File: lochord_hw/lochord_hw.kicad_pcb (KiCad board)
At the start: 2 copper layers, 29 x 51.9 mm, 21 parts, among them J1 TYPE-C-31-M-12, J2 Conn_01x20_Pin, J3 Conn_01x20_Pin, SW1 TS-1088-AR02016, SW2 TS-1088-AR02016, U2 ESP32-S3-WROOM-1, U3 LD1117S33TR_SOT223

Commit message: atomic14 pcb design
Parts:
- removed D1: RED, LED_SMD:LED_0603_1608Metric
- removed D2: GREEN, LED_SMD:LED_0603_1608Metric
- removed J2, J3: Conn_01x20_Pin, Connector_PinHeader_2.54mm:PinHeader_1x20_P2.54mm_Vertical
- removed the R5 at (131.8, 69.5)
- added C6: 100nF, Capacitor_SMD:C_0603_1608Metric, F.Cu at (85.7, 87.0)
- added R10: 10K, Resistor_SMD:R_0603_1608Metric, F.Cu at (169.0, 62.3)
- added R11: 10K, Resistor_SMD:R_0603_1608Metric, F.Cu at (169.0, 64.8)
- added R12: 10K, Resistor_SMD:R_0603_1608Metric, F.Cu at (169.0, 67.3)
- added R13: 10K, Resistor_SMD:R_0603_1608Metric, F.Cu at (169.0, 69.9)
- added R14: 10K, Resistor_SMD:R_0603_1608Metric, F.Cu at (169.0, 72.4)
- added R6: 10K, Resistor_SMD:R_0603_1608Metric, F.Cu at (165.0, 67.3)
- added R7: 10K, Resistor_SMD:R_0603_1608Metric, F.Cu at (165.0, 69.9)
- added R8: 10K, Resistor_SMD:R_0603_1608Metric, F.Cu at (165.0, 72.4)
- added R9: 10K, Resistor_SMD:R_0603_1608Metric, F.Cu at (165.0, 74.9)
- added SW10: SW_Push, Switch_Keyboard_Kailh:SW_Kailh_Choc_V2_1.50u, F.Cu at (180.0, 83.5)
- added SW11: SW_Push, Switch_Keyboard_Kailh:SW_Kailh_Choc_V2_1.00u, F.Cu at (204.0, 83.5)
- added SW12: SW_Push, Switch_Keyboard_Kailh:SW_Kailh_Choc_V2_1.50u, F.Cu at (228.5, 83.5)
- added SW13: UI_Encoder, Rotary_Encoder:RotaryEncoder_Alps_EC11E-Switch_Vertical_H20mm_CircularMountingHoles, F.Cu at (117.2, 64.5)
- added SW14: SW_Push, Switch_Keyboard_Kailh:SW_Kailh_Choc_V2_1.00u, F.Cu at (98.5, 67.5)
- added SW15: UI_Encoder, Rotary_Encoder:RotaryEncoder_Alps_EC11E-Switch_Vertical_H20mm_CircularMountingHoles, F.Cu at (128.2, 85.5)
- added SW3: UI_Encoder, Rotary_Encoder:RotaryEncoder_Alps_EC11E-Switch_Vertical_H20mm_CircularMountingHoles, F.Cu at (139.2, 64.5)
- added SW6: SW_Push, Switch_Keyboard_Kailh:SW_Kailh_Choc_V2_2.25u_90deg, F.Cu at (175.0, 114.5)
- added SW7: SW_Push, Switch_Keyboard_Kailh:SW_Kailh_Choc_V2_2.25u_90deg, F.Cu at (194.5, 114.5)
- added SW8: SW_Push, Switch_Keyboard_Kailh:SW_Kailh_Choc_V2_2.25u_90deg, F.Cu at (233.5, 114.5)
- added SW9: SW_Push, Switch_Keyboard_Kailh:SW_Kailh_Choc_V2_2.25u_90deg, F.Cu at (214.0, 114.5)
- C1: value 10u -> 10uF
- C2: value 22u -> 22uF
- C3: value 100n -> 100nF
- C4: value 10u -> 100nF
- C5: value 10u -> 1uF
- D3: value BLUE -> RED
- R3, R4: value 5.1K -> 10K
- R5: renamed from R6; value 5.1K -> 1K
- U2: value ESP32-S3-WROOM-1 -> ESP32-S3-WROOM-1-N8R8
- moved C2 65.2 mm to (95.2, 128.4), turned to 90 degrees
- moved C1 63.9 mm to (100.3, 128.4), turned to 90 degrees
- moved C3 63.6 mm to (97.8, 128.4), turned to 90 degrees
- moved C4 55.7 mm to (102.6, 127.1)
- moved U3 53.2 mm to (97.8, 121.9)
- moved U2 52.8 mm to (97.8, 95.2)
- moved J1 52.8 mm to (98.1, 135.8)
- moved R1 52.8 mm to (104.3, 129.5)
- moved R2 52.8 mm to (91.6, 129.4)
- moved SW1 52.8 mm to (89.8, 134.0)
- moved D3 52.8 mm to (99.3, 111.8)
- moved R5 52.8 mm to (102.7, 111.8)
- moved SW2 52.8 mm to (106.1, 134.0)
- moved R3 52.5 mm to (86.5, 92.7), turned to 0 degrees
- moved C5 48.6 mm to (85.7, 89.5)
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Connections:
- R4 pad 1: +5V -> +3V3
- R4 pad 2: Net-(D1-A) -> GPIO0
- R5 pad 1: GPIO21 -> +3V3
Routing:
- net GPIO18: track 17.1 -> 322.7 mm, vias 1 -> 11
- net GPIO47: track 26.5 -> 202.7 mm, vias 1 -> 11
- net GPIO48: track 23.4 -> 176.0 mm, vias 1 -> 5
- net GPIO8: track 17.8 -> 139.6 mm, vias 1 -> 6
- net GPIO40: track 11.2 -> 129.8 mm, vias 0 -> 3
- net GPIO14: track 32.6 -> 140.7 mm, vias 1 -> 2
- net GPIO16: track 12.5 -> 108.4 mm
- net GPIO42: track 8.73 -> 104.3 mm, vias 0 -> 3
- net GPIO17: track 15.9 -> 109.6 mm, vias 1 -> 2
- net GPIO15: track 11.0 -> 101.1 mm
- net GPIO45: track 20.5 -> 108.7 mm, vias 1 -> 2
- net GPIO13: track 35.7 -> 122.7 mm, vias 1 -> 2
- net GPIO21: track 30.5 -> 113.5 mm, vias 1 -> 2
- net GPIO7: track 10.0 -> 90.8 mm, vias 0 -> 6
- net GPIO41: track 10.0 -> 80.8 mm, vias 0 -> 1
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- added copper zone on F.Cu, net +3V3
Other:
- board size 29 x 51.9 mm -> 161.6 x 82.3 mm

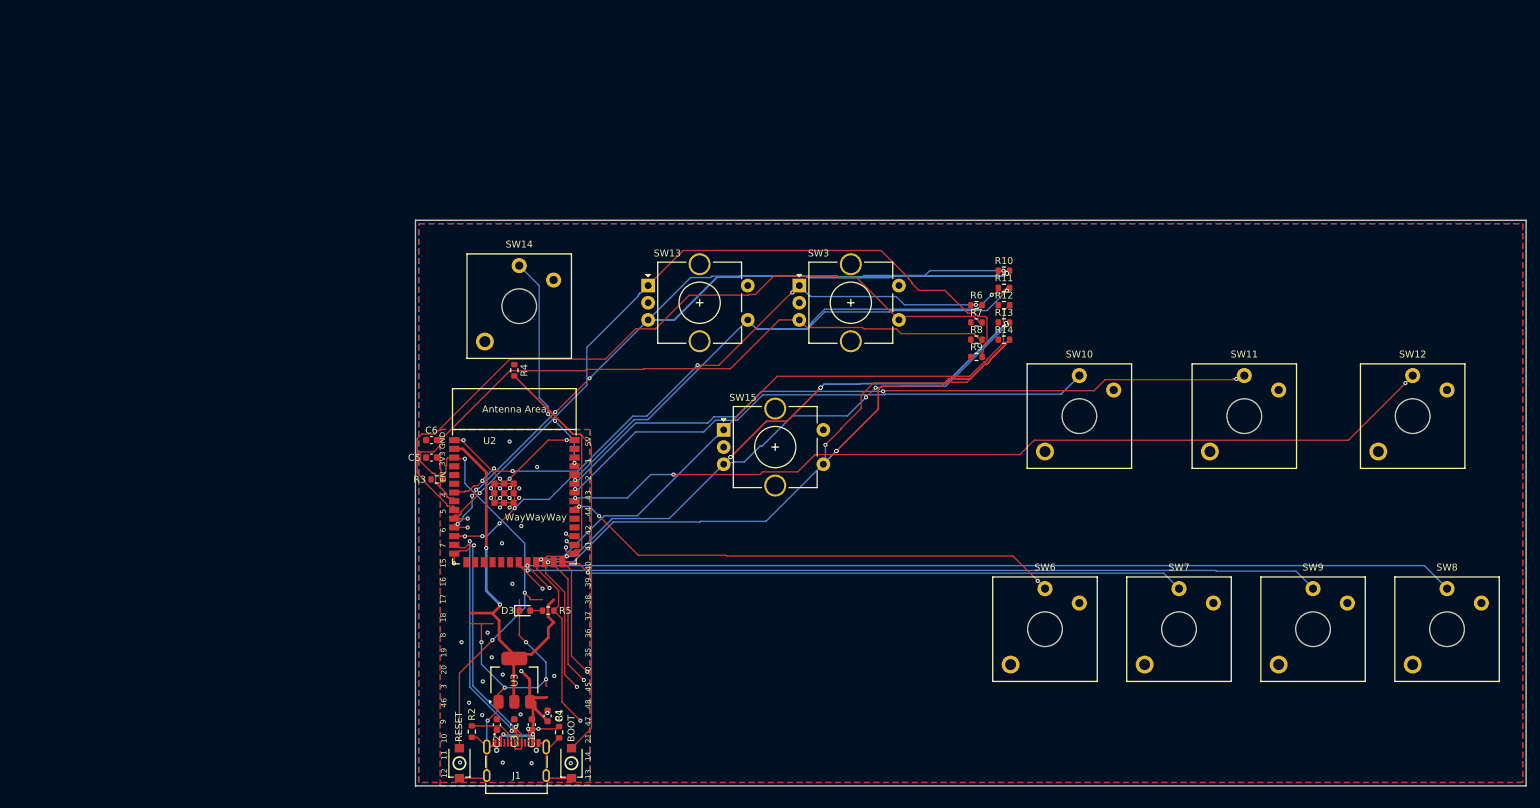
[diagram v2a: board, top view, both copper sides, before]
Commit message: hw: pcb design for esp32-p4
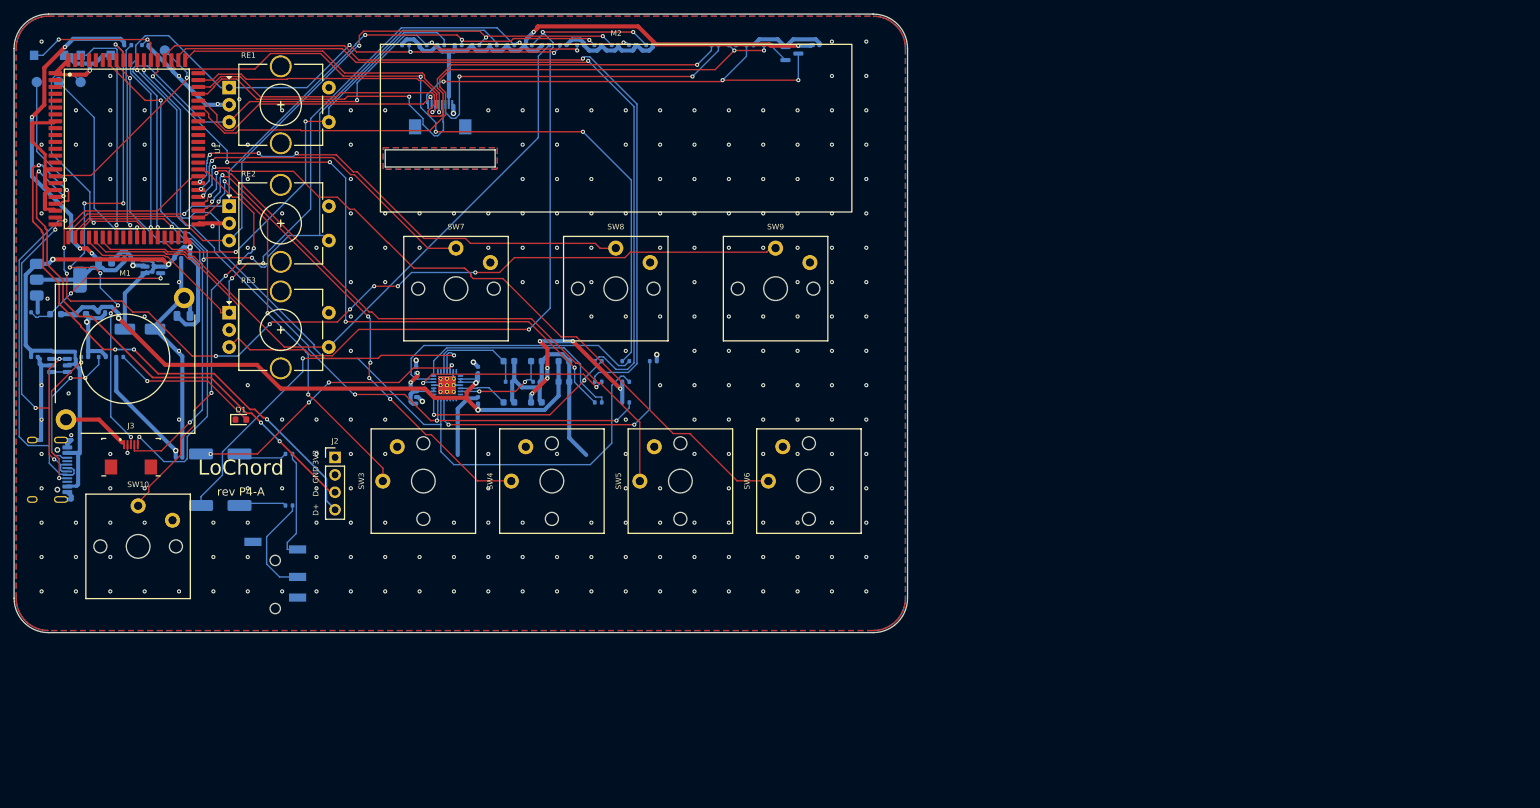
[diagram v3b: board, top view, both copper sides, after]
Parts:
- removed D3: RED, LED_SMD:LED_0603_1608Metric
- removed SW11, SW14: SW_Push, Switch_Keyboard_Kailh:SW_Kailh_Choc_V2_1.00u
- removed SW12: SW_Push, Switch_Keyboard_Kailh:SW_Kailh_Choc_V2_1.50u
- removed SW13, SW15: UI_Encoder, Rotary_Encoder:RotaryEncoder_Alps_EC11E-Switch_Vertical_H20mm_CircularMountingHoles
- added C10: 100nF, Capacitor_SMD:C_0402_1005Metric, B.Cu at (37.8, 68.4)
- added C11: 100nF, Capacitor_SMD:C_0402_1005Metric, B.Cu at (141.7, 29.5)
- added C12: 10uF, Capacitor_SMD:C_0603_1608Metric, B.Cu at (101.0, 81.5)
- added C13: 100nF, Capacitor_SMD:C_0402_1005Metric, B.Cu at (83.5, 76.8)
- added C14: 100nF, Capacitor_SMD:C_0402_1005Metric, B.Cu at (83.5, 81.2)
- added C15: 10uF, Capacitor_SMD:C_0603_1608Metric, B.Cu at (105.0, 75.5)
- added C16: 100nF, Capacitor_SMD:C_0402_1005Metric, B.Cu at (92.5, 76.8)
- added C17: 10uF, Capacitor_SMD:C_0603_1608Metric, B.Cu at (105.0, 78.5)
- added C18: 100nF, Capacitor_SMD:C_0402_1005Metric, B.Cu at (92.5, 81.2)
- added C19: 10uF, Capacitor_SMD:C_0603_1608Metric, B.Cu at (97.0, 75.5)
- added C20: 100nF, Capacitor_SMD:C_0402_1005Metric, B.Cu at (97.0, 78.5)
- added C21: 10uF, Capacitor_SMD:C_0603_1608Metric, B.Cu at (97.0, 81.5)
- added C22: 10uF, Capacitor_SMD:C_0603_1608Metric, B.Cu at (101.0, 75.5)
- added C23: 100nF, Capacitor_SMD:C_0402_1005Metric, B.Cu at (101.0, 78.5)
- added C24: 220uF/6.3V, Capacitor_SMD:CP_Elec_6.3x5.4, B.Cu at (55.0, 89.0)
- added C25: 220uF/6.3V, Capacitor_SMD:CP_Elec_6.3x5.4, B.Cu at (55.0, 96.5)
- added C26: 100nF, Capacitor_SMD:C_0402_1005Metric, B.Cu at (49.0, 89.5)
- added C27: 10nF, Capacitor_SMD:C_0402_1005Metric, B.Cu at (104.9, 29.5)
- added C28: 10nF, Capacitor_SMD:C_0402_1005Metric, B.Cu at (107.4, 29.5)
- added C29: 10nF, Capacitor_SMD:C_0402_1005Metric, B.Cu at (109.9, 29.5)
- added C30: 10nF, Capacitor_SMD:C_0402_1005Metric, B.Cu at (112.4, 29.5)
- added C31: 10nF, Capacitor_SMD:C_0402_1005Metric, B.Cu at (114.9, 29.5)
- added C32: 10nF, Capacitor_SMD:C_0402_1005Metric, B.Cu at (117.5, 29.5)
- added C7: 1uF, Capacitor_SMD:C_0402_1005Metric, B.Cu at (48.8, 60.5)
- added C8: 1uF, Capacitor_SMD:C_0402_1005Metric, B.Cu at (28.0, 68.4)
- added C9: 10uF, Capacitor_SMD:C_0603_1608Metric, B.Cu at (34.7, 68.7)
- added D1: GREEN, LED_SMD:LED_0603_1608Metric, F.Cu at (58.0, 84.0)
- added FB1: 600R@100MHz, Inductor_SMD:L_0603_1608Metric, B.Cu at (31.0, 68.7)
- added J2: DEBUG USJ, Connector_PinHeader_2.54mm:PinHeader_1x04_P2.54mm_Vertical, F.Cu at (71.7, 89.5)
- added J3: JOYSTICK_NS, lochord:FPC_1x05_P0.50mm_Horizontal_ZIF, F.Cu at (42.0, 89.5)
- added J4: LCD_NV3007, lochord:FPC_1x08_P0.50mm_Horizontal_ZIF, B.Cu at (87.0, 40.0)
- added J5: PJ-320D, Connector_Audio:Jack_3.5mm_PJ320D_Horizontal, B.Cu at (63.0, 106.7)
- added M1: JOYSTICK_NS_MODULE, lochord:Joystick_NintendoSwitch_Module, F.Cu at (41.1, 75.2)
- added M2: NV3007_2.79in_428x142, lochord:Display_NV3007_2.79in_428x142, F.Cu at (112.6, 41.6)
- added Q1: SI2302, Package_TO_SOT_SMD:SOT-23, B.Cu at (138.2, 30.7)
- added R15: 0R, Resistor_SMD:R_0402_1005Metric, B.Cu at (129.5, 29.5)
- added R16: 100k, Resistor_SMD:R_0402_1005Metric, B.Cu at (132.1, 29.5)
- added R17: 100R, Resistor_SMD:R_0402_1005Metric, B.Cu at (134.6, 29.5)
- added R18: 33R, Resistor_SMD:R_0402_1005Metric, B.Cu at (110.0, 75.5)
- added R19: 33R, Resistor_SMD:R_0402_1005Metric, B.Cu at (110.0, 78.5)
- added R20: 33R, Resistor_SMD:R_0402_1005Metric, B.Cu at (110.0, 81.5)
- added R21: 33R, Resistor_SMD:R_0402_1005Metric, B.Cu at (114.0, 75.5)
- added R22: 4.7k, Resistor_SMD:R_0402_1005Metric, B.Cu at (114.0, 78.5)
- added R23: 4.7k, Resistor_SMD:R_0402_1005Metric, B.Cu at (114.0, 81.5)
- added R24: 10k, Resistor_SMD:R_0402_1005Metric, B.Cu at (118.0, 75.5)
- added R25: 10R, Resistor_SMD:R_0402_1005Metric, B.Cu at (65.0, 89.0)
- added R26: 10R, Resistor_SMD:R_0402_1005Metric, B.Cu at (65.0, 96.5)
- added RE1: EC11E15244G1, Rotary_Encoder:RotaryEncoder_Alps_EC11E-Switch_Vertical_H20mm_CircularMountingHoles, F.Cu at (56.3, 35.7)
- added RE2: EC11E15244G1, Rotary_Encoder:RotaryEncoder_Alps_EC11E-Switch_Vertical_H20mm_CircularMountingHoles, F.Cu at (56.3, 53.0)
- added RE3: EC11E15244G1, Rotary_Encoder:RotaryEncoder_Alps_EC11E-Switch_Vertical_H20mm_CircularMountingHoles, F.Cu at (56.3, 68.5)
- added SW4: CHORD2, Switch_Keyboard_Kailh:SW_Kailh_Choc_V1_2.00u, F.Cu at (103.2, 93.0)
- added SW5: CHORD3, Switch_Keyboard_Kailh:SW_Kailh_Choc_V1_2.00u, F.Cu at (122.0, 93.0)
- added TP1: USB_HS_DM, TestPoint:TestPoint_Pad_D1.5mm, B.Cu at (46.9, 30.3)
- added TP2: USB_HS_DP, TestPoint:TestPoint_Pad_D1.5mm, B.Cu at (28.3, 34.9)
- added TP3: U0TXD, TestPoint:TestPoint_Pad_D1.5mm, B.Cu at (31.5, 34.9)
- added TP4: U0RXD, TestPoint:TestPoint_Pad_D1.5mm, B.Cu at (34.7, 34.9)
- added U1: WT0132P4-A1-N16R32, lochord:WT0132P4-A1, F.Cu at (41.4, 44.6)
- added U4: USBLC6-2SC6, Package_TO_SOT_SMD:SOT-23-6, B.Cu at (31.6, 76.1)
- added U5: ES8388, lochord:QFN-28-1EP_4x4mm_P0.45mm_EP2.6x2.6mm_ThermalVias, B.Cu at (88.0, 79.0)
- C1: value 10uF -> 1uF; footprint Capacitor_SMD:C_0603_1608Metric -> Capacitor_SMD:C_0402_1005Metric; moved to B.Cu
- C2: value 22uF -> 100uF/10V; footprint Capacitor_SMD:C_0603_1608Metric -> Capacitor_SMD:CP_Elec_5x5.4; moved to B.Cu
- C3: value 100nF -> 22uF/25V; footprint Capacitor_SMD:C_0603_1608Metric -> Capacitor_SMD:C_0805_2012Metric; moved to B.Cu
- C4, C6: footprint Capacitor_SMD:C_0603_1608Metric -> Capacitor_SMD:C_0402_1005Metric; moved to B.Cu
- C5: value 1uF -> 22uF/25V; footprint Capacitor_SMD:C_0603_1608Metric -> Capacitor_SMD:C_0805_2012Metric; moved to B.Cu
- J1: value TYPE-C-31-M-12 -> USB-C 16P; footprint TYPE-C-31-M-12:HRO_TYPE-C-31-M-12 -> Connector_USB:USB_C_Receptacle_HRO_TYPE-C-31-M-12; moved to B.Cu
- R1: value 5.1K -> 10k; footprint Resistor_SMD:R_0603_1608Metric -> Resistor_SMD:R_0402_1005Metric; moved to B.Cu
- R10, R11, R12, R13, R6, R7, R8, R9: value 10K -> 10k; footprint Resistor_SMD:R_0603_1608Metric -> Resistor_SMD:R_0402_1005Metric; moved to B.Cu
- R14: value 10K -> 22R; footprint Resistor_SMD:R_0603_1608Metric -> Resistor_SMD:R_0402_1005Metric; moved to B.Cu
- R2: value 5.1K -> 5.1k; footprint Resistor_SMD:R_0603_1608Metric -> Resistor_SMD:R_0402_1005Metric; moved to B.Cu
- R3: value 10K -> 5.1k; footprint Resistor_SMD:R_0603_1608Metric -> Resistor_SMD:R_0402_1005Metric; moved to B.Cu
- R4: value 10K -> 470R; footprint Resistor_SMD:R_0603_1608Metric -> Resistor_SMD:R_0402_1005Metric; moved to B.Cu
- R5: value 1K -> 10k; footprint Resistor_SMD:R_0603_1608Metric -> Resistor_SMD:R_0402_1005Metric; moved to B.Cu
- SW1: value TS-1088-AR02016 -> EN; footprint easyeda2kicad:SW-SMD_L3.9-W3.0-P4.45 -> lochord:SW_SMD_TS-1088-AR02016_3.9x3.0mm; moved to B.Cu
- SW10: value SW_Push -> LOOP; footprint Switch_Keyboard_Kailh:SW_Kailh_Choc_V2_1.50u -> Switch_Keyboard_Kailh:SW_Kailh_Choc_V1_1.00u
- SW2: value TS-1088-AR02016 -> BOOT; footprint easyeda2kicad:SW-SMD_L3.9-W3.0-P4.45 -> lochord:SW_SMD_TS-1088-AR02016_3.9x3.0mm; moved to B.Cu
- SW3: value UI_Encoder -> CHORD1; footprint Rotary_Encoder:RotaryEncoder_Alps_EC11E-Switch_Vertical_H20mm_CircularMountingHoles -> Switch_Keyboard_Kailh:SW_Kailh_Choc_V1_2.00u
- SW6: value SW_Push -> CHORD4; footprint Switch_Keyboard_Kailh:SW_Kailh_Choc_V2_2.25u_90deg -> Switch_Keyboard_Kailh:SW_Kailh_Choc_V1_2.00u
- SW7: value SW_Push -> CHORD5; footprint Switch_Keyboard_Kailh:SW_Kailh_Choc_V2_2.25u_90deg -> Switch_Keyboard_Kailh:SW_Kailh_Choc_V1_1.50u
- SW8: value SW_Push -> CHORD6; footprint Switch_Keyboard_Kailh:SW_Kailh_Choc_V2_2.25u_90deg -> Switch_Keyboard_Kailh:SW_Kailh_Choc_V1_1.00u
- SW9: value SW_Push -> CHORD7; footprint Switch_Keyboard_Kailh:SW_Kailh_Choc_V2_2.25u_90deg -> Switch_Keyboard_Kailh:SW_Kailh_Choc_V1_1.50u
- U2: value ESP32-S3-WROOM-1-N8R8 -> AMS1117-3.3; footprint PCM_Espressif:ESP32-S3-WROOM-1 -> Package_TO_SOT_SMD:SOT-223-3_TabPin2; moved to B.Cu
- U3: value LD1117S33TR_SOT223 -> LP5907MFX-3.3; footprint Package_TO_SOT_SMD:SOT-223-3_TabPin2 -> Package_TO_SOT_SMD:SOT-23-5; moved to B.Cu
- moved SW10 138.3 mm to (43.0, 102.5)
- moved SW8 130.7 mm to (112.5, 65.0)
- moved SW2 124.1 mm to (36.9, 31.0), turned to 0 degrees
- moved SW1 119.1 mm to (30.1, 31.0), turned to 0 degrees
- moved R1 118.0 mm to (41.6, 29.5), turned to 0 degrees
- moved SW7 116.3 mm to (89.3, 65.0)
- moved C1 113.8 mm to (44.1, 29.5), turned to 0 degrees
- moved SW9 92.6 mm to (135.8, 65.0)
- moved C4 91.1 mm to (28.0, 74.9), turned to 0 degrees
- moved R6 89.0 mm to (84.5, 29.5)
- moved R7 87.8 mm to (87.1, 29.5)
- moved R8 86.7 mm to (89.6, 29.5)
- moved R9 85.8 mm to (92.2, 29.5)
- moved R5 84.9 mm to (82.0, 29.5), turned to 0 degrees
- moved J1 82.4 mm to (28.7, 91.3), turned to 90 degrees
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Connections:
- net Net-(J1-CC1) renamed /USB_CC1
- C1 pad 1: +3V3 -> /EN
- C2 pad 1: +3V3 -> +5V
- C3 pad 1: +3V3 -> +5V
- C5 pad 1: EN -> +3V3
- C6 pad 1: GND -> +3V3
- C6 pad 2: +3V3 -> GND
- J1 pad A6: D+ -> /USB_DP
- J1 pad A7: D- -> /USB_DM
- J1 pad B5: Net-(J1-CC2) -> /USB_CC2
- J1 pad B6: D+ -> /USB_DP
- J1 pad B7: D- -> /USB_DM
- R1 pad 1: Net-(J1-CC2) -> +3V3
- R1 pad 2: GND -> /BOOTSEL
- R10 pad 2: GPIO18 -> /ENC2_SW
- R11 pad 2: GPIO8 -> /ENC3_A
- R12 pad 2: GPIO21 -> /ENC3_B
- R13 pad 2: GPIO47 -> /ENC3_SW
- R14 pad 1: +3V3 -> /LCD_SCLK
- R14 pad 2: GPIO48 -> /LCD_SCLK_R
- R3 pad 1: +3V3 -> /USB_CC2
- R3 pad 2: EN -> GND
- R4 pad 2: GPIO0 -> /PWR_LED
- R5 pad 2: Net-(D3-A) -> /ENC1_A
- R6 pad 2: GPIO7 -> /ENC1_B
- R7 pad 2: GPIO16 -> /ENC1_SW
- R8 pad 2: GPIO15 -> /ENC2_A
- R9 pad 2: GPIO17 -> /ENC2_B
- SW1 pad 1: GND -> /EN
- SW1 pad 2: EN -> GND
- SW10 pad 1: GPIO41 -> /KEY_LOOP
- SW2 pad 1: GND -> /BOOT
- SW2 pad 2: GPIO0 -> GND
- SW6 pad 1: GPIO39 -> /KEY4
- SW7 pad 1: GPIO45 -> /KEY5
- SW8 pad 1: GPIO14 -> /KEY6
- SW9 pad 1: GPIO13 -> /KEY7
- U2 pad 3: EN -> +5V
- U3 pad 1: GND -> +5V
- U3 pad 2: +3V3 -> GND
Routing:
- net GPIO18: track 322.7 -> 0.00 mm, vias 11 -> 0
- net GPIO47: track 202.7 -> 0.00 mm, vias 11 -> 0
- net GPIO48: track 176.0 -> 0.00 mm, vias 5 -> 0
- net /KEY7: track 0.00 -> 144.9 mm, vias 0 -> 8
- net GPIO14: track 140.7 -> 0.00 mm, vias 2 -> 0
- net +3V3: track 57.0 -> 197.6 mm, vias 2 -> 16
- net /ENC3_B: track 0.00 -> 140.3 mm, vias 0 -> 3
- net GPIO8: track 139.6 -> 0.00 mm, vias 6 -> 0
- net GPIO40: track 129.8 -> 0.00 mm, vias 3 -> 0
- net /I2C_SDA: track 0.00 -> 125.2 mm, vias 0 -> 1
- net GPIO13: track 122.7 -> 0.00 mm, vias 2 -> 0
- net GND: track 110.6 -> 230.3 mm, vias 38 -> 251
- net /I2S_BCLK: track 0.00 -> 119.3 mm, vias 0 -> 1
- net /I2S_MCLK: track 0.00 -> 115.4 mm, vias 0 -> 1
- net GPIO21: track 113.5 -> 0.00 mm, vias 2 -> 0
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- added copper zone on In2.Cu, net +3V3
- added copper zone on In1.Cu, net GND
- removed copper zone on F.Cu, net +3V3
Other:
- board size 161.6 x 82.3 mm -> 130 x 90 mm
- copper layers 2 -> 4
- rule pad_to_mask_clearance: 0 -> 0.05
- board text added: "D+"
- board text added: "D-"
- board text added: "LoChord"
- board text added: "LoChord rev P4-A"
- board text added: "rev P4-A"
- board text removed: "0"
- board text removed: "1"
- board text removed: "10"
- board text removed: "11"
- board text removed: "12"
- board text removed: "13"
- board text removed: "14"
- board text removed: "15"
- board text removed: "16"
- board text removed: "17"
- board text removed: "18"
- board text removed: "19"
- board text removed: "2"
- board text removed: "20"
- board text removed: "21"
- board text removed: "3"
- board text removed: "35"
- board text removed: "36"
- board text removed: "37"
- board text removed: "38"
- board text removed: "39"
- board text removed: "4"
- board text removed: "40"
- board text removed: "41"
- board text removed: "42"
- board text removed: "43"
- board text removed: "44"
- board text removed: "45"
- board text removed: "46"
- board text removed: "47"
- board text removed: "48"
- board text removed: "5"
- board text removed: "5V"
- board text removed: "6"
- board text removed: "7"
- board text removed: "8"
- board text removed: "9"
- board text removed: "BOOT"
- board text removed: "EN"
- board text removed: "RESET"
- board text removed: "WayWayWay"
